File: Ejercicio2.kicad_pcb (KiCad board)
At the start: 4 copper layers, 14 parts, among them J1 DB9, U1 AMIS42665TJAA1RG, U2 RS232CESE

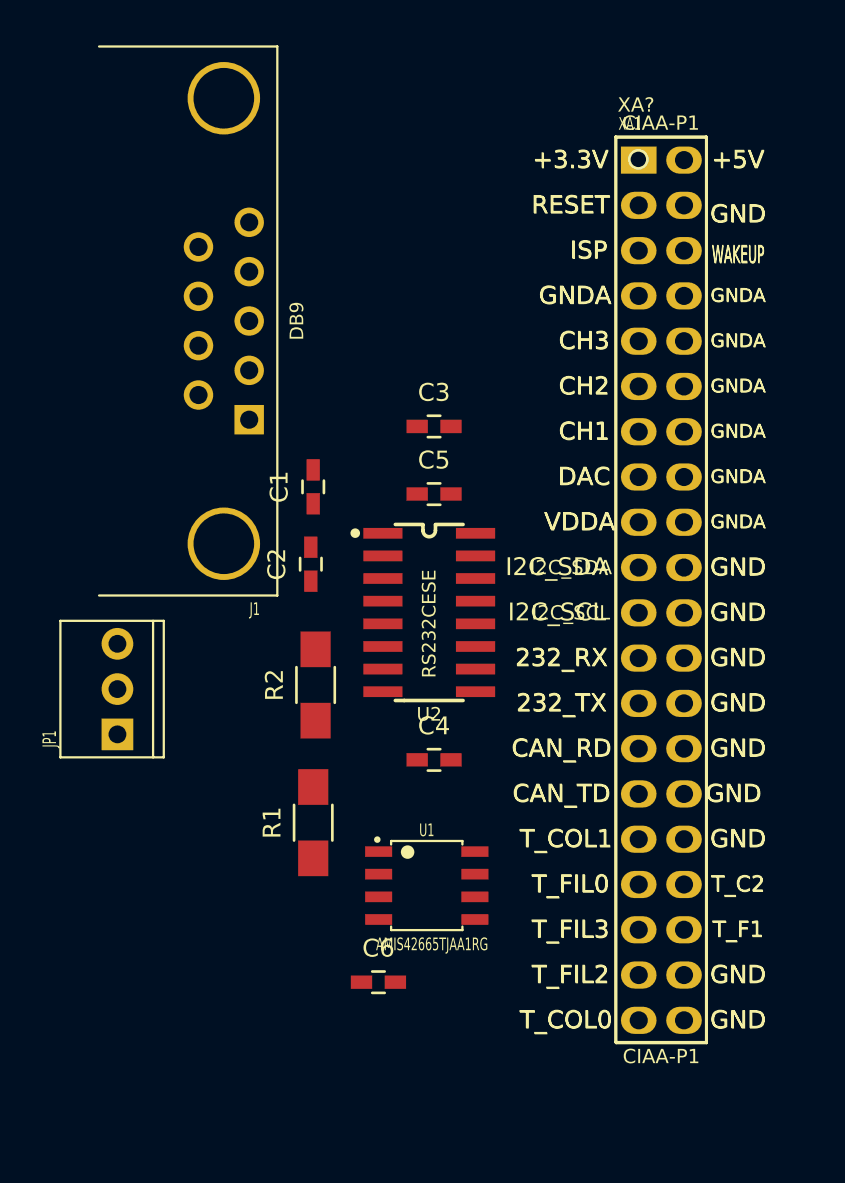
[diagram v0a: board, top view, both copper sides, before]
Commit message: Actualizaciones ejercicio 29 de mayo 2017
Definición de las Capas para 3V, 5V y GND.
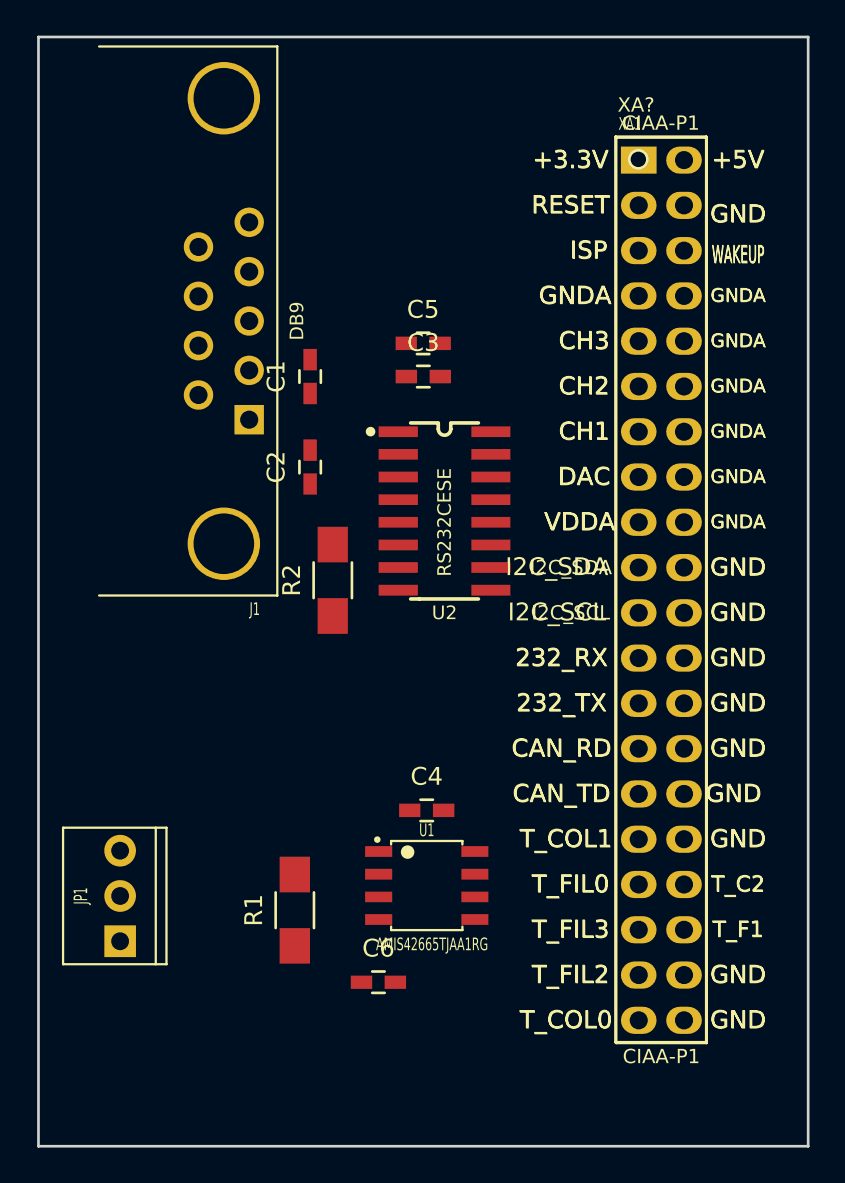
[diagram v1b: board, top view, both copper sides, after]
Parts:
- moved JP1 11.6 mm to (88.4, 102.8)
- moved C5 8.48 mm to (105.4, 71.8)
- moved C1 6.19 mm to (99.1, 73.7)
- moved R2 5.95 mm to (100.3, 85.1)
- moved U2 5.76 mm to (106.6, 81.2)
- moved C2 5.45 mm to (99.1, 78.7)
- moved R1 5.02 mm to (98.2, 103.6)
- moved C4 2.86 mm to (105.6, 98.0)
- moved C3 2.86 mm to (105.4, 73.7)
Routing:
- added copper zone on POWER, net +3V3
- added copper zone on POWER, net +5V
- added copper zone on GND, net GND
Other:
- board outline added: 43.2 x 62.2 mm
- net class Default: clearance 0.2 -> 0.3
- rule trace_clearance: 0.2 -> 0.3
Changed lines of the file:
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@@
   (general
     (links 46)
-    (no_connects 46)
-    (area 78.655259 54.850619 126.002461 116.360621)
+    (no_connects 33)
+    (area 83.744999 54.534999 127.075001 116.915001)
     (thickness 1.6)
-    (drawings 0)
+    (drawings 4)
     (tracks 0)
     (zones 0)
@@
     (2 POWER power)
     (31 BOT mixed)
-    (33 F.Adhes user)
-    (35 F.Paste user)
+    (33 F.Adhes user hide)
+    (35 F.Paste user hide)
     (37 F.SilkS user)
-    (39 F.Mask user)
+    (39 F.Mask user hide)
     (40 Dwgs.User user)
-    (41 Cmts.User user)
-    (42 Eco1.User user)
-    (43 Eco2.User user)
+    (41 Cmts.User user hide)
+    (42 Eco1.User user hide)
+    (43 Eco2.User user hide)
     (44 Edge.Cuts user)
-    (45 Margin user)
-    (47 F.CrtYd user)
-    (49 F.Fab user)
+    (45 Margin user hide)
+    (47 F.CrtYd user hide)
+    (49 F.Fab user hide)
   )
   (setup
     (last_trace_width 0.25)
-    (trace_clearance 0.2)
+    (user_trace_width 0.3)
+    (trace_clearance 0.3)
     (zone_clearance 0.508)
     (zone_45_only no)
@@
     (via_min_size 0.4)
     (via_min_drill 0.3)
+    (user_via 1.27 0.7)
     (uvia_size 0.3)
     (uvia_drill 0.1)
@@
   (net 46 "Net-(XA1-Pad39)")
   (net_class Default "Esta es la clase de red por defecto."
-    (clearance 0.2)
+    (clearance 0.3)
     (trace_width 0.25)
     (via_dia 0.6)
@@
   )
   (module ej2:C_0603_HandSoldering (layer TOP)
-    (at 99.23272 79.84744 90)
+    (at 99.06 73.66 90)
     (descr "Capacitor SMD 0603, hand soldering")
     (tags "capacitor 0603")
@@
   )
   (module ej2:C_0603_HandSoldering (layer TOP)
-    (at 99.0981 84.18576 90)
+    (at 99.06 78.74 90)
     (descr "Capacitor SMD 0603, hand soldering")
     (tags "capacitor 0603")
@@
   )
   (module ej2:C_0603_HandSoldering (layer TOP)
-    (at 106.01198 76.45908)
+    (at 105.41 73.66)
     (descr "Capacitor SMD 0603, hand soldering")
     (tags "capacitor 0603")
@@
       (effects (font (size 1 1) (thickness 0.15)))
     )
-    (fp_text value 100nF (at 0 1.9) (layer F.Fab)
+    (fp_text value 100nF (at 4.89 3.52) (layer F.Fab)
       (effects (font (size 1 1) (thickness 0.15)))
     )
@@
   )
   (module ej2:C_0603_HandSoldering (layer TOP)
-    (at 106.01198 95.16618)
+    (at 105.6 98)
     (descr "Capacitor SMD 0603, hand soldering")
     (tags "capacitor 0603")
@@
   )
   (module ej2:C_0603_HandSoldering (layer TOP)
-    (at 106.01198 80.25384)
+    (at 105.4 71.8)
     (descr "Capacitor SMD 0603, hand soldering")
     (tags "capacitor 0603")
@@
       (effects (font (size 1 1) (thickness 0.15)))
     )
-    (fp_text value 100nF (at 0 1.9) (layer F.Fab)
+    (fp_text value 100nF (at 5.09 0.59) (layer F.Fab)
       (effects (font (size 1 1) (thickness 0.15)))
     )
@@
   )
   (module ej2:CON_PALETA_3 (layer TOP)
-    (at 88.24976 91.19362 90)
-    (fp_text reference JP1 (at -2.8 -3.8 90) (layer F.SilkS)
+    (at 88.4 102.8 90)
+    (fp_text reference JP1 (at 0 -2.2 90) (layer F.SilkS)
       (effects (font (size 0.762 0.4572) (thickness 0.127)))
     )
@@
   )
   (module ej2:R_1206_HandSoldering (layer TOP)
-    (at 99.23272 98.68916 90)
+    (at 98.2 103.6 90)
     (descr "Resistor SMD 1206, hand soldering")
     (tags "resistor 1206")
@@
   )
   (module ej2:R_1206_HandSoldering (layer TOP)
-    (at 99.36734 90.96248 90)
+    (at 100.33 85.09 90)
     (descr "Resistor SMD 1206, hand soldering")
     (tags "resistor 1206")
@@
   )
   (module ej2:SP3232ECN-SOIC16N (layer TOP)
-    (at 105.7402 86.89594 270)
+    (at 106.6 81.2 270)
     (descr "SMALL OUTLINE INTEGRATED CIRCUIT")
     (tags "SMALL OUTLINE INTEGRATED CIRCUIT")
@@
     (fp_line (start 3.81 -1.27) (end -1.27 -1.27) (layer F.SilkS) (width 0.15))
   )
+  (gr_line (start 83.82 116.84) (end 127 116.84) (angle 90) (layer Edge.Cuts) (width 0.15))
+  (gr_line (start 83.82 54.61) (end 83.82 116.84) (angle 90) (layer Edge.Cuts) (width 0.15))
+  (gr_line (start 127 54.61) (end 83.82 54.61) (angle 90) (layer Edge.Cuts) (width 0.15))
+  (gr_line (start 127 116.84) (end 127 54.61) (angle 90) (layer Edge.Cuts) (width 0.15))
+  (zone (net 3) (net_name +3V3) (layer POWER) (hatch edge 0.508)
+    (priority 1)
+    (connect_pads (clearance 0.508))
+    (min_thickness 0.254)
+    (fill yes (arc_segments 16) (thermal_gap 0.508) (thermal_bridge_width 0.508))
+    (polygon
+      (pts
+        (xy 118.8 90.8) (xy 118.8 55.2) (xy 118.8 53.2) (xy 82.8 53.2) (xy 83 91)
+      )
+    )
+  )
+  (zone (net 2) (net_name +5V) (layer POWER) (hatch edge 0.508)
+    (connect_pads (clearance 0.508))
+    (min_thickness 0.254)
+    (fill yes (arc_segments 16) (thermal_gap 0.508) (thermal_bridge_width 0.508))
+    (polygon
+      (pts
+        (xy 77.4 49.6) (xy 131 49.6) (xy 131 121.2) (xy 77 121) (xy 76.8 121)
+      )
+    )
+  )
+  (zone (net 1) (net_name GND) (layer GND) (hatch edge 0.508)
+    (connect_pads (clearance 0.508))
+    (min_thickness 0.254)
+    (fill yes (arc_segments 16) (thermal_gap 0.508) (thermal_bridge_width 0.508))
+    (polygon
+      (pts
+        (xy 71.6 45) (xy 71.2 125.8) (xy 140 126.2) (xy 140.2 45.2)
+      )
+    )
+  )
 )
